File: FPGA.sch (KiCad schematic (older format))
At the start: 0 parts

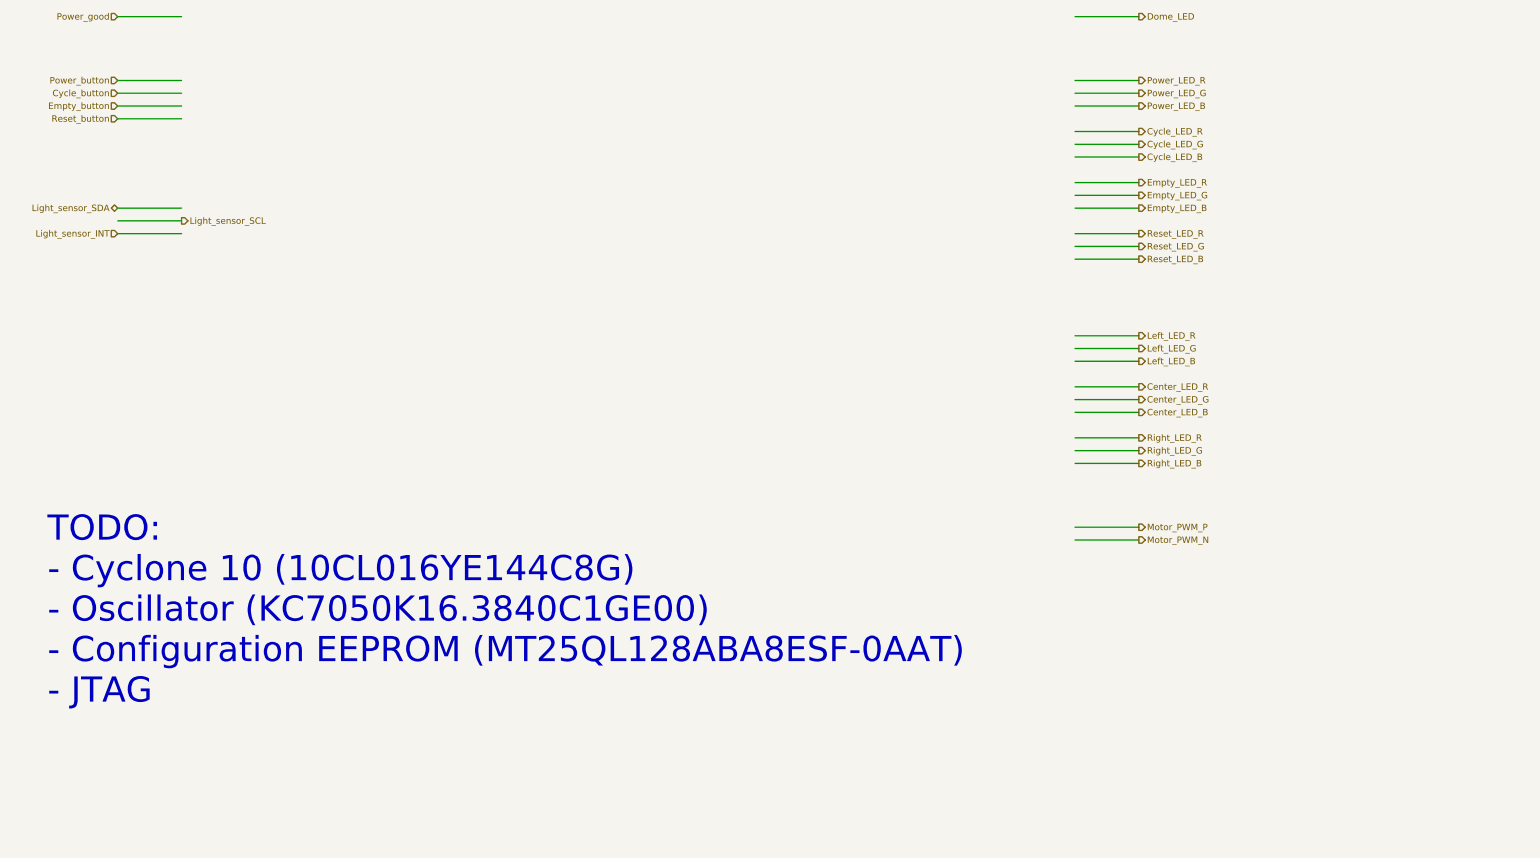
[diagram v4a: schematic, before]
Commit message: Add support components for the FPGA
- Configuration EEPROM
- 20 MHz oscillator
- JTAG debug port connector
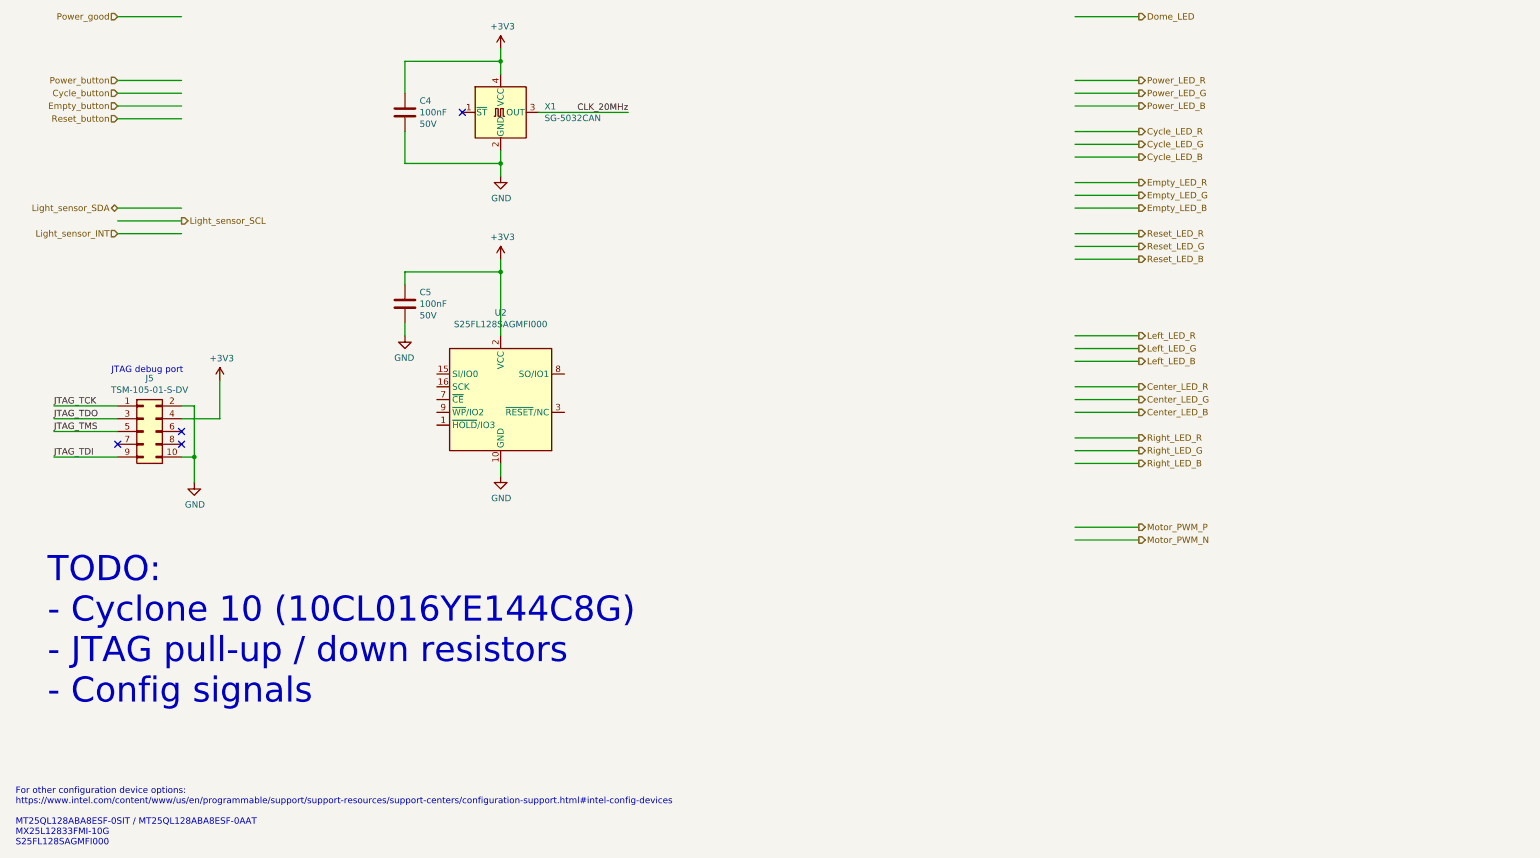
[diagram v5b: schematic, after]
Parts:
- added C4, C5: 100nF, Capacitor_SMD:C_0603_1608Metric, symbol Device:C
- added J5: TSM-105-01-S-DV, Connector_PinHeader_2.54mm:PinHeader_2x05_P2.54mm_Vertical_SMD, symbol Connector_Generic:Conn_02x05_Odd_Even
- added U2: S25FL128SAGMFI000, Package_SO:SOIC-16W_7.5x10.3mm_P1.27mm, symbol Memory_Flash:IS25WP256D-xM
- added X1: SG-5032CAN, Oscillator:Oscillator_SMD_SeikoEpson_SG8002CA-4Pin_7.0x5.0mm, symbol Oscillator:SG-5032CAN
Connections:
- net labels added: +3V3, CLK_20MHz, GND, JTAG_TCK, JTAG_TDI, JTAG_TDO, JTAG_TMS
- wire segments 32 -> 57
- no-connect marks 0 -> 4
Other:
- note added: "For other configuration device options:\nhttps://www.intel.com/content/www/us/en/programmable/support/support-resources/support-centers/configuration-support.html#intel-config-devices\n\nMT25QL128ABA8ESF-0SIT / MT25QL128ABA8ESF-0AAT\nMX25L12833FMI-10G\nS25FL128SAGMFI000"
- note added: "JTAG debug port"
- note added: "TODO:\n- Cyclone 10 (10CL016YE144C8G)\n- JTAG pull-up / down resistors\n- Config signals"
- note removed: "TODO:\n- Cyclone 10 (10CL016YE144C8G)\n- Oscillator (KC7050K16.3840C1GE00)\n- Configuration EEPROM (MT25QL128ABA8ESF-0AAT)\n- JTAG"
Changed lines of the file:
@@
 Motor_PWM_P
 Text Notes 950  6400 0    197  ~ 0
-TODO:\n- Cyclone 10 (10CL016YE144C8G)\n- Oscillator (KC7050K16.3840C1GE00)\n- Configuration EEPROM (MT25QL128ABA8ESF-0AAT)\n- JTAG
+TODO:\n- Cyclone 10 (10CL016YE144C8G)\n- JTAG pull-up / down resistors\n- Config signals
 Wire Wire Line
 	9000 1000 9500 1000
@@
 Wire Wire Line
 	1500 2600 2000 2600
+$Comp
+L Oscillator:SG-5032CAN X1
+U 1 1 605F8FC0
+P 4500 1750
+F 0 "X1" H 4844 1796 50  0000 L CNN
+F 1 "SG-5032CAN" H 4844 1705 50  0000 L CNN
+F 2 "Oscillator:Oscillator_SMD_SeikoEpson_SG8002CA-4Pin_7.0x5.0mm" H 5200 1400 50  0001 C CNN
+F 3 "https://support.epson.biz/td/api/doc_check.php?dl=brief_SG5032CAN&lang=en" H 4400 1750 50  0001 C CNN
+F 4 "X1G0044510011" H 4500 1750 50  0001 C CNN "Part_number"
+	1    4500 1750
+	1    0    0    -1
+$EndComp
+$Comp
+L Device:C C?
+U 1 1 605FB521
+P 3750 1750
+AR Path="/603F20AB/605FB521" Ref="C?"  Part="1"
+AR Path="/60624089/605FB521" Ref="C?"  Part="1"
+AR Path="/603F1F4D/605FB521" Ref="C4"  Part="1"
+F 0 "C4" H 3865 1841 50  0000 L CNN
+F 1 "100nF" H 3865 1750 50  0000 L CNN
+F 2 "Capacitor_SMD:C_0603_1608Metric" H 3788 1600 50  0001 C CNN
+F 3 "~" H 3750 1750 50  0001 C CNN
+F 4 "C1608X5R1H104K080AA" H 3750 1750 50  0001 C CNN "Part_Number"
+F 5 "50V" H 3865 1659 50  0000 L CNN "Voltage"
+	1    3750 1750
+	1    0    0    -1
+$EndComp
+Wire Wire Line
+	3750 2150 3750 1900
+$Comp
+L power:GND #PWR?
+U 1 1 605FDDD4
+P 4500 2250
+AR Path="/605FDDD4" Ref="#PWR?"  Part="1"
+AR Path="/60624089/605FDDD4" Ref="#PWR?"  Part="1"
+AR Path="/603F1F4D/605FDDD4" Ref="#PWR056"  Part="1"
+F 0 "#PWR056" H 4500 2000 50  0001 C CNN
+F 1 "GND" H 4505 2077 50  0000 C CNN
+F 2 "" H 4500 2250 50  0001 C CNN
+F 3 "" H 4500 2250 50  0001 C CNN
+	1    4500 2250
+	1    0    0    -1
+$EndComp
+$Comp
+L power:+3V3 #PWR?
+U 1 1 605FDDDA
+P 4500 1250
+AR Path="/605FDDDA" Ref="#PWR?"  Part="1"
+AR Path="/60624089/605FDDDA" Ref="#PWR?"  Part="1"
+AR Path="/603F1F4D/605FDDDA" Ref="#PWR055"  Part="1"
+F 0 "#PWR055" H 4500 1100 50  0001 C CNN
+F 1 "+3V3" H 4515 1423 50  0000 C CNN
+F 2 "" H 4500 1250 50  0001 C CNN
+F 3 "" H 4500 1250 50  0001 C CNN
+	1    4500 1250
+	1    0    0    -1
+$EndComp
+Wire Wire Line
+	4500 2050 4500 2150
+Connection ~ 4500 1350
+Wire Wire Line
+	4500 1350 4500 1450
+Wire Wire Line
+	4500 2150 3750 2150
+Connection ~ 4500 2150
+Wire Wire Line
+	4500 2150 4500 2250
+Wire Wire Line
+	4500 1250 4500 1350
+Wire Wire Line
+	3750 1600 3750 1350
+Wire Wire Line
+	3750 1350 4500 1350
+NoConn ~ 4200 1750
+Text Label 5500 1750 2    50   ~ 0
+CLK_20MHz
+Wire Wire Line
+	4800 1750 5500 1750
+$Comp
+L Memory_Flash:IS25WP256D-xM U2
+U 1 1 60607F43
+P 4500 4000
+F 0 "U2" H 4500 4681 50  0000 C CNN
+F 1 "S25FL128SAGMFI000" H 4500 4590 50  0000 C CNN
+F 2 "Package_SO:SOIC-16W_7.5x10.3mm_P1.27mm" H 4550 4600 50  0001 C CNN
+F 3 "https://www.cypress.com/file/448601/download" H 4550 3500 50  0001 C CNN
+F 4 "S25FL128SAGMFI000" H 4500 4000 50  0001 C CNN "Part_number"
+	1    4500 4000
+	1    0    0    -1
+$EndComp
+$Comp
+L power:GND #PWR?
+U 1 1 60611D96
+P 4500 4600
+AR Path="/60611D96" Ref="#PWR?"  Part="1"
+AR Path="/60624089/60611D96" Ref="#PWR?"  Part="1"
+AR Path="/603F1F4D/60611D96" Ref="#PWR058"  Part="1"
+F 0 "#PWR058" H 4500 4350 50  0001 C CNN
+F 1 "GND" H 4505 4427 50  0000 C CNN
+F 2 "" H 4500 4600 50  0001 C CNN
+F 3 "" H 4500 4600 50  0001 C CNN
+	1    4500 4600
+	1    0    0    -1
+$EndComp
+$Comp
+L power:+3V3 #PWR?
+U 1 1 60611D9C
+P 4500 2900
+AR Path="/60611D9C" Ref="#PWR?"  Part="1"
+AR Path="/60624089/60611D9C" Ref="#PWR?"  Part="1"
+AR Path="/603F1F4D/60611D9C" Ref="#PWR057"  Part="1"
+F 0 "#PWR057" H 4500 2750 50  0001 C CNN
+F 1 "+3V3" H 4515 3073 50  0000 C CNN
+F 2 "" H 4500 2900 50  0001 C CNN
+F 3 "" H 4500 2900 50  0001 C CNN
+	1    4500 2900
+	1    0    0    -1
+$EndComp
+Wire Wire Line
+	4500 4600 4500 4500
+$Comp
+L power:GND #PWR?
+U 1 1 6061DDDC
+P 3750 3500
+AR Path="/6061DDDC" Ref="#PWR?"  Part="1"
+AR Path="/60624089/6061DDDC" Ref="#PWR?"  Part="1"
+AR Path="/603F1F4D/6061DDDC" Ref="#PWR054"  Part="1"
+F 0 "#PWR054" H 3750 3250 50  0001 C CNN
+F 1 "GND" H 3755 3327 50  0000 C CNN
+F 2 "" H 3750 3500 50  0001 C CNN
+F 3 "" H 3750 3500 50  0001 C CNN
+	1    3750 3500
+	-1   0    0    -1
+$EndComp
+Wire Wire Line
+	4500 3000 4500 3500
+Wire Wire Line
+	3750 3000 4500 3000
+Wire Wire Line
+	3750 3500 3750 3400
+Wire Wire Line
+	3750 3100 3750 3000
+Wire Wire Line
+	4500 2900 4500 3000
+Connection ~ 4500 3000
+$Comp
+L Device:C C?
+U 1 1 606267AF
+P 3750 3250
+AR Path="/603F20AB/606267AF" Ref="C?"  Part="1"
+AR Path="/60624089/606267AF" Ref="C?"  Part="1"
+AR Path="/603F1F4D/606267AF" Ref="C5"  Part="1"
+F 0 "C5" H 3865 3341 50  0000 L CNN
+F 1 "100nF" H 3865 3250 50  0000 L CNN
+F 2 "Capacitor_SMD:C_0603_1608Metric" H 3788 3100 50  0001 C CNN
+F 3 "~" H 3750 3250 50  0001 C CNN
+F 4 "C1608X5R1H104K080AA" H 3750 3250 50  0001 C CNN "Part_Number"
+F 5 "50V" H 3865 3159 50  0000 L CNN "Voltage"
+	1    3750 3250
+	1    0    0    -1
+$EndComp
+Text Notes 700  7500 0    50   ~ 0
+For other configuration device options:\nhttps://www.intel.com/content/www/us/en/programmable/support/support-resources/support-centers/configuration-support.html#intel-config-devices\n\nMT25QL128ABA8ESF-0SIT / MT25QL128ABA8ESF-0AAT\nMX25L12833FMI-10G\nS25FL128SAGMFI000
+$Comp
+L Connector_Generic:Conn_02x05_Odd_Even J5
+U 1 1 60629DD9
+P 1700 4250
+F 0 "J5" H 1750 4667 50  0000 C CNN
+F 1 "TSM-105-01-S-DV" H 1750 4576 50  0000 C CNN
+F 2 "Connector_PinHeader_2.54mm:PinHeader_2x05_P2.54mm_Vertical_SMD" H 1700 4250 50  0001 C CNN
+F 3 "https://suddendocs.samtec.com/catalog_english/tsm.pdf" H 1700 4250 50  0001 C CNN
+F 4 "TSM-105-01-S-DV" H 1700 4250 50  0001 C CNN "Part_number"
+	1    1700 4250
+	1    0    0    -1
+$EndComp
+Text Notes 1450 3800 0    50   ~ 0
+JTAG debug port
+Text Label 1000 4150 0    50   ~ 0
+JTAG_TDO
+Wire Wire Line
+	1000 4150 1500 4150
+Wire Wire Line
+	2000 4050 2100 4050
+Wire Wire Line
+	1000 4050 1500 4050
+Text Label 1000 4050 0    50   ~ 0
+JTAG_TCK
+Wire Wire Line
+	1000 4250 1500 4250
+Text Label 1000 4250 0    50   ~ 0
+JTAG_TMS
+$Comp
+L power:GND #PWR?
+U 1 1 60657302
+P 2100 4650
+AR Path="/60657302" Ref="#PWR?"  Part="1"
+AR Path="/60624089/60657302" Ref="#PWR?"  Part="1"
+AR Path="/603F1F4D/60657302" Ref="#PWR052"  Part="1"
+F 0 "#PWR052" H 2100 4400 50  0001 C CNN
+F 1 "GND" H 2105 4477 50  0000 C CNN
+F 2 "" H 2100 4650 50  0001 C CNN
+F 3 "" H 2100 4650 50  0001 C CNN
+	1    2100 4650
+	1    0    0    -1
+$EndComp
+Wire Wire Line
+	2100 4050 2100 4450
+$Comp
+L power:+3V3 #PWR?
+U 1 1 6065AC53
+P 2300 3850
+AR Path="/6065AC53" Ref="#PWR?"  Part="1"
+AR Path="/60624089/6065AC53" Ref="#PWR?"  Part="1"
+AR Path="/603F1F4D/6065AC53" Ref="#PWR053"  Part="1"
+F 0 "#PWR053" H 2300 3700 50  0001 C CNN
+F 1 "+3V3" H 2315 4023 50  0000 C CNN
+F 2 "" H 2300 3850 50  0001 C CNN
+F 3 "" H 2300 3850 50  0001 C CNN
+	1    2300 3850
+	1    0    0    -1
+$EndComp
+Wire Wire Line
+	2000 4150 2300 4150
+Wire Wire Line
+	2300 3850 2300 4150
+NoConn ~ 2000 4250
+NoConn ~ 2000 4350
+NoConn ~ 1500 4350
+Text Label 1000 4450 0    50   ~ 0
+JTAG_TDI
+Wire Wire Line
+	2000 4450 2100 4450
+Connection ~ 2100 4450
+Wire Wire Line
+	2100 4450 2100 4650
+Wire Wire Line
+	1500 4450 1000 4450
 $EndSCHEMATC

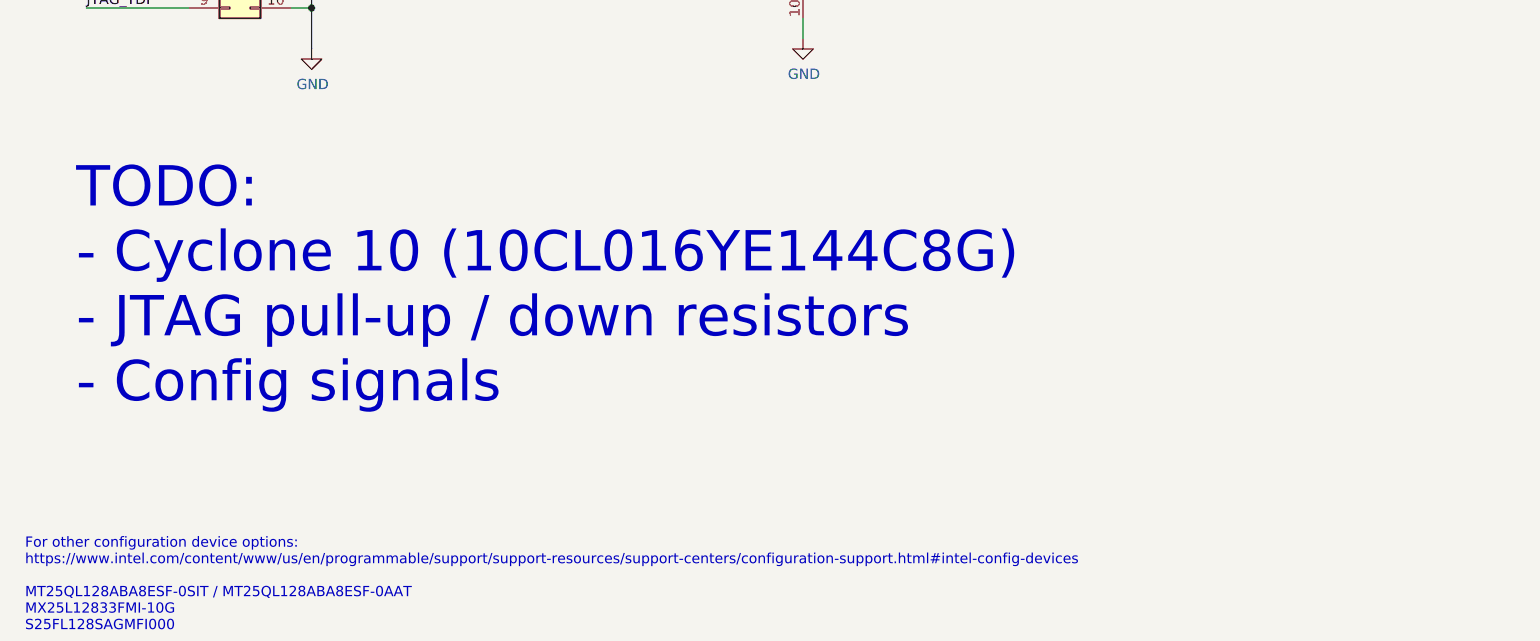
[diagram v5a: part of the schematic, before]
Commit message: Update the TODO lists
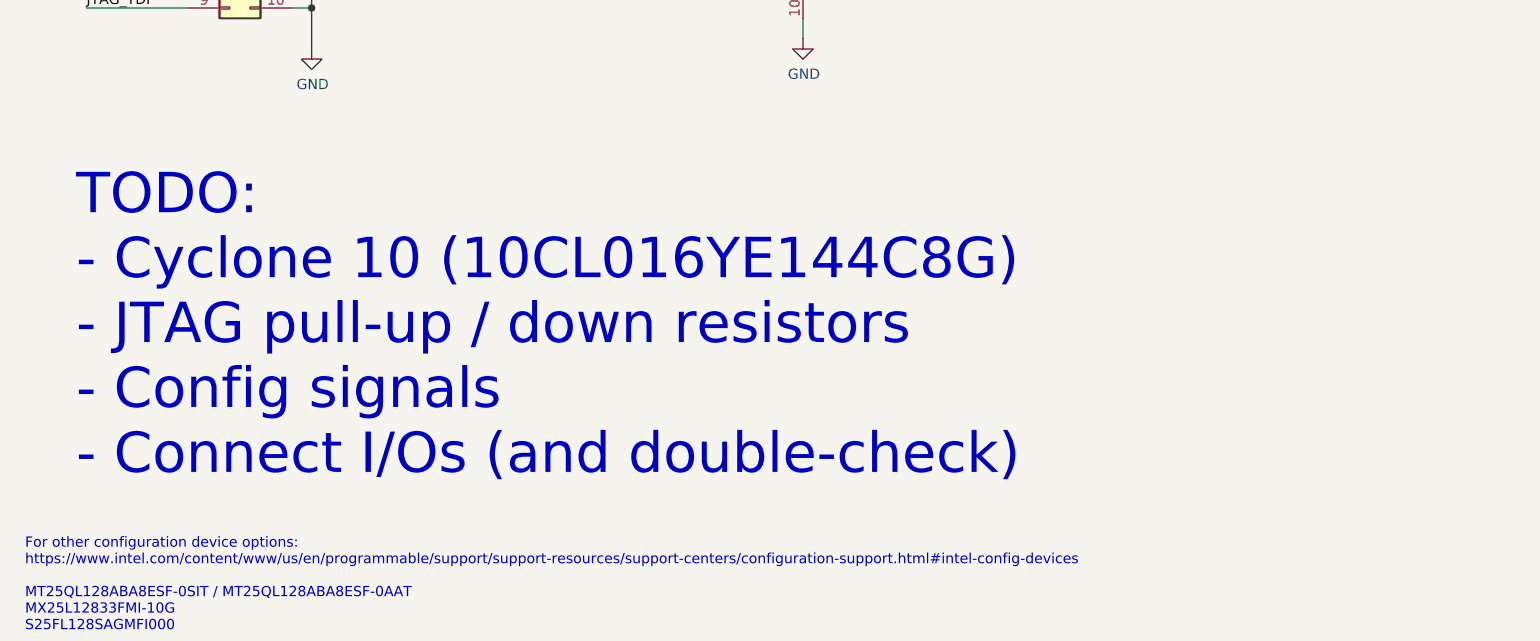
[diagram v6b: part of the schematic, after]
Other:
- note added: "TODO:\n- Cyclone 10 (10CL016YE144C8G)\n- JTAG pull-up / down resistors\n- Config signals\n- Connect I/Os (and double-check)"
- note removed: "TODO:\n- Cyclone 10 (10CL016YE144C8G)\n- JTAG pull-up / down resistors\n- Config signals"
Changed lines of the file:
@@
 Text HLabel 9500 5000 2    50   Output ~ 0
 Motor_PWM_P
-Text Notes 950  6400 0    197  ~ 0
-TODO:\n- Cyclone 10 (10CL016YE144C8G)\n- JTAG pull-up / down resistors\n- Config signals
+Text Notes 950  6750 0    197  ~ 0
+TODO:\n- Cyclone 10 (10CL016YE144C8G)\n- JTAG pull-up / down resistors\n- Config signals\n- Connect I/Os (and double-check)
 Wire Wire Line
 	9000 1000 9500 1000
